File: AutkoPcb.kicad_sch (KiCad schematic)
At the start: 17 parts, among them J101 JST 2.56mm, J102 JST 2.56mm, J103 JST 2.56mm, J104 JST 2.56mm, J105 JST 2.56mm, J107 JST 2.56mm, J108 JST 2.56mm, J109 JST 2.56mm, J110 JST 2.56mm, J111 JST 2.56mm, J112 JST 2.56mm, J113 JST 2.56mm, J114 Conn_01x12_Pin

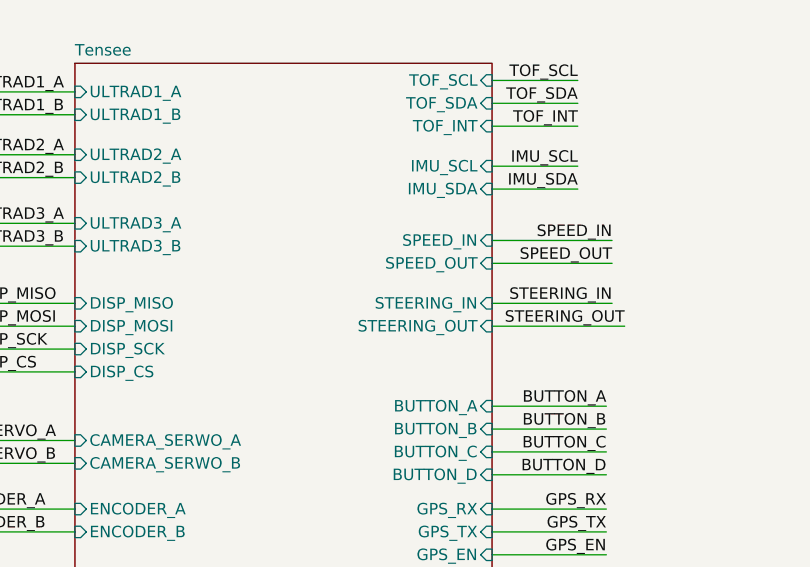
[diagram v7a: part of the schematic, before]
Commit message: [FEAT] Zaktualizowano układ do debauncing
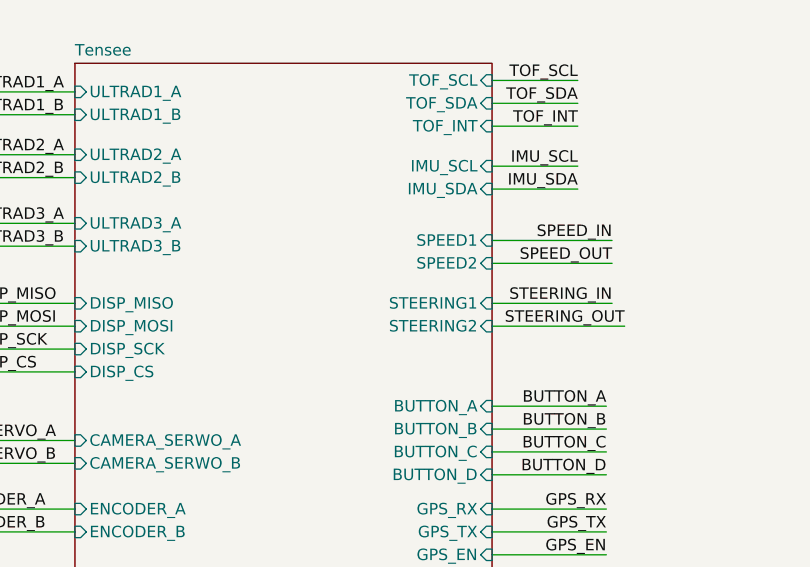
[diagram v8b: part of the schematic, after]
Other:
- sheet Tensee ports: added SPEED1, SPEED2, STEERING1, STEERING2; removed SPEED_IN, SPEED_OUT, STEERING_IN, STEERING_OUT
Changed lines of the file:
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@@
-      (effects (font (size 1.27 1.27)) (justify right))
-    )
-    (pin "SPEED_IN" input (at 184.785 39.37 0)
-      (effects (font (size 1.27 1.27)) (justify right))
-    )
-    (pin "STEERING_IN" input (at 184.785 46.355 0)
-      (effects (font (size 1.27 1.27)) (justify right))
-    )
-    (pin "SPEED_OUT" input (at 184.785 41.91 0)
-      (effects (font (size 1.27 1.27)) (justify right))
-    )
-    (pin "STEERING_OUT" input (at 184.785 48.895 0)
       (effects (font (size 1.27 1.27)) (justify right))
     )
@@
       (effects (font (size 1.27 1.27)) (justify right))
     )
+    (pin "STEERING2" input (at 184.785 48.895 0)
+      (effects (font (size 1.27 1.27)) (justify right))
+    )
+    (pin "STEERING1" input (at 184.785 46.355 0)
+      (effects (font (size 1.27 1.27)) (justify right))
+    )
+    (pin "SPEED1" input (at 184.785 39.37 0)
+      (effects (font (size 1.27 1.27)) (justify right))
+    )
+    (pin "SPEED2" input (at 184.785 41.91 0)
+      (effects (font (size 1.27 1.27)) (justify right))
+    )
